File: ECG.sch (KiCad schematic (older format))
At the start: 14 parts, among them P1 MountingHole_Pad, P2 MountingHole_Pad, P3 MountingHole_Pad, U1 ADR4525, U2 L7805

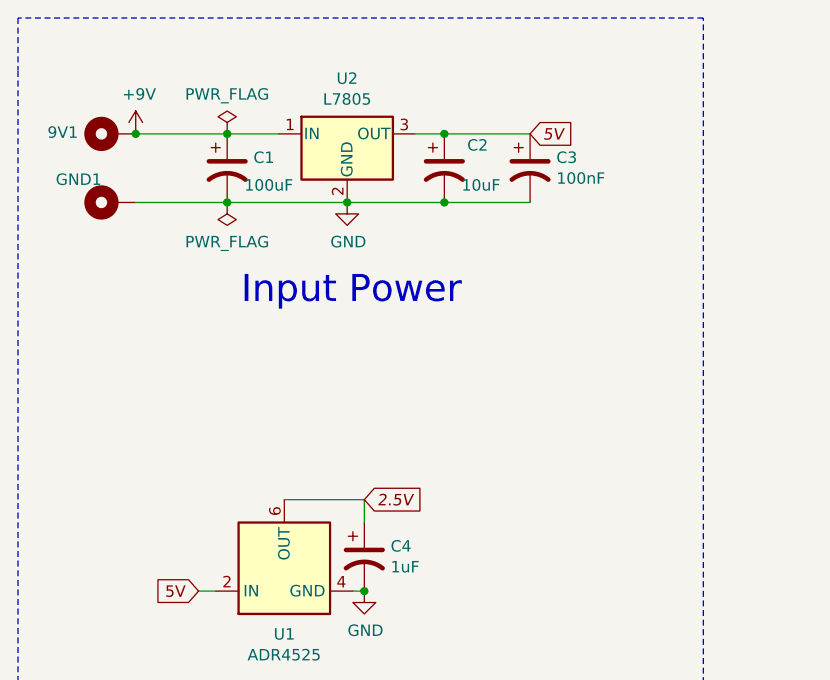
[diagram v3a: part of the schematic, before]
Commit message: Added battery circuit
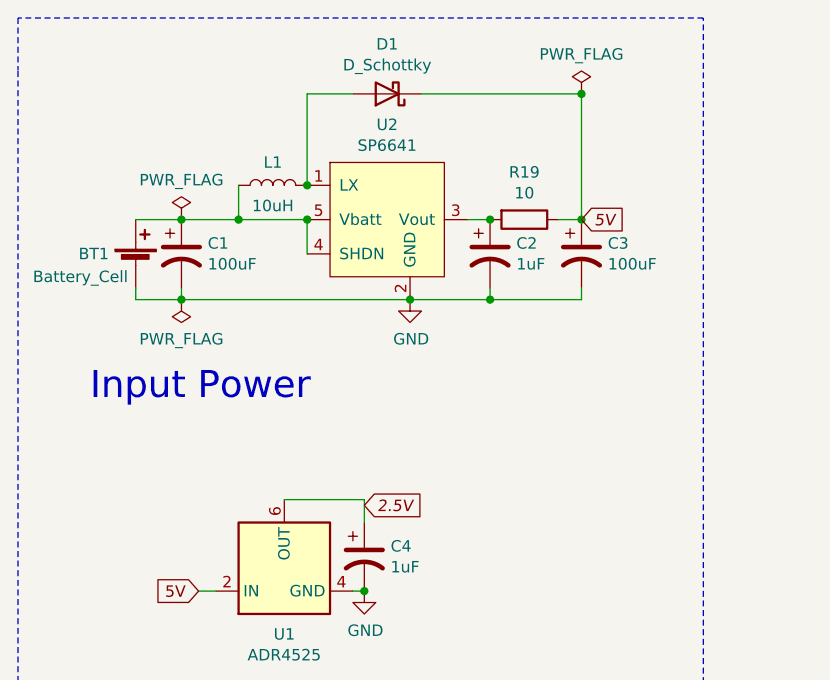
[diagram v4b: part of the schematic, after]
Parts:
- removed 9V1: MountingHole_Pad, MountingHole:MountingHole_6.5mm_Pad_Via, symbol Mechanical:MountingHole_Pad
- removed GND1: MountingHole_Pad, MountingHole:MountingHole_6mm_Pad_Via, symbol Mechanical:MountingHole_Pad
- removed U2: L7805, Package_TO_SOT_THT:TO-220-3_Horizontal_TabDown, symbol Regulator_Linear:L7805
- added BT1: Battery_Cell, symbol Device:Battery_Cell
- added D1: D_Schottky, Diode_SMD:D_SOD-323_HandSoldering, symbol Device:D_Schottky
- added L1: 10uH, symbol Device:L
- added R19: 10, Resistor_SMD:R_0805_2012Metric_Pad1.15x1.40mm_HandSolder, symbol Device:R
- added U2: SP6641, symbol Regulators:SP6641
- C1: footprint Capacitor_SMD:CP_Elec_6.3x3 -> Capacitor_SMD:C_0805_2012Metric_Pad1.15x1.40mm_HandSolder
- C2: value 10uF -> 1uF; footprint Capacitor_SMD:CP_Elec_5x5.3 -> Capacitor_SMD:C_0805_2012Metric_Pad1.15x1.40mm_HandSolder
- C3: value 100nF -> 100uF
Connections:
- net 5V: now also D1.1 (K), R19.1; no longer C2.1
- net GND: now also BT1.2 (-), U2.2 (GND)
- net +9V: no longer names the net of C1.1
- net +9V: now also BT1.1 (+), L1.1, U2.4 (SHDN), U2.5 (Vbatt)
- new net: D1.2 (A), L1.2, U2.1 (LX)
- new net: C2.1, R19.2, U2.3 (Vout)
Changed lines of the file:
@@
 Comment4 ""
 $EndDescr
-$Comp
-L Device:CP1 C2
-U 1 1 5F980DB6
-P 2750 2425
-F 0 "C2" H 2850 2525 50  0000 L CNN
-F 1 "10uF" H 2825 2350 50  0000 L CNN
-F 2 "Capacitor_SMD:CP_Elec_5x5.3" H 2750 2425 50  0001 C CNN
-F 3 "https://www.illinoiscapacitor.com/pdf/seriesDocuments/AXZ%20series.pdf" H 2750 2425 50  0001 C CNN
-	1    2750 2425
-	1    0    0    -1
-$EndComp
-$Comp
-L Device:CP1 C3
-U 1 1 5F9833A5
-P 3125 2425
-F 0 "C3" H 3240 2471 50  0000 L CNN
-F 1 "100nF" H 3240 2380 50  0000 L CNN
-F 2 "Capacitor_SMD:C_0805_2012Metric_Pad1.15x1.40mm_HandSolder" H 3125 2425 50  0001 C CNN
-F 3 "~" H 3125 2425 50  0001 C CNN
-	1    3125 2425
-	1    0    0    -1
-$EndComp
-$Comp
-L Mechanical:MountingHole_Pad 9V1
-U 1 1 5F985E28
-P 1300 2275
-F 0 "9V1" V 1306 2427 50  0000 L CNN
-F 1 "MountingHole_Pad" V 1400 2233 50  0001 L CNN
-F 2 "MountingHole:MountingHole_6.5mm_Pad_Via" H 1300 2275 50  0001 C CNN
-F 3 "~" H 1300 2275 50  0001 C CNN
-	1    1300 2275
-	0    -1   -1   0
-$EndComp
-$Comp
-L Mechanical:MountingHole_Pad GND1
-U 1 1 5F98A564
-P 1300 2575
-F 0 "GND1" V 1400 2624 50  0000 L CNN
-F 1 "MountingHole_Pad" V 1400 2533 50  0001 L CNN
-F 2 "MountingHole:MountingHole_6mm_Pad_Via" H 1300 2575 50  0001 C CNN
-F 3 "~" H 1300 2575 50  0001 C CNN
-	1    1300 2575
-	0    -1   -1   0
-$EndComp
-Text Notes 1861 3030 0    118  ~ 0
+Text Notes 1200 3450 0    118  ~ 0
 Input Power
 Text Notes 1733 4734 0    50   ~ 0
@@
 Wire Notes Line
 	885  1768 885  1998
-$Comp
-L power:GND #PWR0102
-U 1 1 5F9A88EF
-P 2325 2575
-F 0 "#PWR0102" H 2325 2325 50  0001 C CNN
-F 1 "GND" H 2330 2402 50  0000 C CNN
-F 2 "" H 2325 2575 50  0001 C CNN
-F 3 "" H 2325 2575 50  0001 C CNN
-	1    2325 2575
-	1    0    0    -1
-$EndComp
-$Comp
-L power:+9V #PWR0101
-U 1 1 5F9AB243
-P 1400 2275
-F 0 "#PWR0101" H 1400 2125 50  0001 C CNN
-F 1 "+9V" H 1415 2448 50  0000 C CNN
-F 2 "" H 1400 2275 50  0001 C CNN
-F 3 "" H 1400 2275 50  0001 C CNN
-	1    1400 2275
-	1    0    0    -1
-$EndComp
-$Comp
-L power:PWR_FLAG #FLG01
-U 1 1 5F9B3B5D
-P 1800 2275
-F 0 "#FLG01" H 1800 2350 50  0001 C CNN
-F 1 "PWR_FLAG" H 1800 2448 50  0000 C CNN
-F 2 "" H 1800 2275 50  0001 C CNN
-F 3 "~" H 1800 2275 50  0001 C CNN
-	1    1800 2275
-	1    0    0    -1
-$EndComp
 $Comp
 L Device:CP1 C4
@@
 	1    0    0    -1
 $EndComp
-$Comp
-L Regulator_Linear:L7805 U2
-U 1 1 5F977B65
-P 2325 2275
-F 0 "U2" H 2325 2517 50  0000 C CNN
-F 1 "L7805" H 2325 2426 50  0000 C CNN
-F 2 "Package_TO_SOT_THT:TO-220-3_Horizontal_TabDown" H 2350 2125 50  0001 L CIN
-F 3 "http://www.st.com/content/ccc/resource/technical/document/datasheet/41/4f/b3/b0/12/d4/47/88/CD00000444.pdf/files/CD00000444.pdf/jcr:content/translations/en.CD00000444.pdf" H 2325 2225 50  0001 C CNN
-	1    2325 2275
-	1    0    0    -1
-$EndComp
-$Comp
-L Device:CP1 C1
-U 1 1 5F97B8CA
-P 1800 2425
-F 0 "C1" H 1915 2471 50  0000 L CNN
-F 1 "100uF" H 1875 2350 50  0000 L CNN
-F 2 "Capacitor_SMD:CP_Elec_6.3x3" H 1800 2425 50  0001 C CNN
-F 3 "https://www.we-online.de/katalog/datasheet/860240575006.pdf" H 1800 2425 50  0001 C CNN
-	1    1800 2425
-	1    0    0    -1
-$EndComp
-Wire Wire Line
-	1400 2575 1800 2575
-Connection ~ 1800 2575
-Wire Wire Line
-	2325 2575 1800 2575
-Connection ~ 2325 2575
-Wire Wire Line
-	1800 2275 1400 2275
-Connection ~ 1800 2275
-Connection ~ 1400 2275
-Wire Wire Line
-	1800 2275 2025 2275
-Wire Wire Line
-	2625 2275 2750 2275
-Wire Wire Line
-	2325 2575 2750 2575
-Wire Wire Line
-	3125 2575 2750 2575
-Connection ~ 2750 2575
-Wire Wire Line
-	3125 2275 2750 2275
-Connection ~ 2750 2275
-Text GLabel 3125 2275 2    50   Input Italic 0
+Text GLabel 3350 2650 2    50   Input Italic 0
 5V
 Wire Wire Line
 	2350 4275 2400 4275
 Connection ~ 2400 4275
-$Comp
-L power:PWR_FLAG #FLG0101
-U 1 1 5F9F7887
-P 1800 2575
-F 0 "#FLG0101" H 1800 2650 50  0001 C CNN
-F 1 "PWR_FLAG" H 1800 2748 50  0000 C CNN
-F 2 "" H 1800 2575 50  0001 C CNN
-F 3 "~" H 1800 2575 50  0001 C CNN
-	1    1800 2575
-	-1   0    0    1
-$EndComp
 $Sheet
 S 6425 2800 950  1425
@@
 F3 "Vin" I L 8375 3500 50
 $EndSheet
-Text GLabel 2400 3875 2    50   Input Italic 0
+Text GLabel 2400 3900 2    50   Input Italic 0
 2.5V
 Wire Wire Line
@@
 	0    1    1    0
 $EndComp
+$Comp
+L Regulators:SP6641 U2
+U 1 1 5FB1FB38
+P 2500 2350
+F 0 "U2" H 2500 2465 50  0000 C CNN
+F 1 "SP6641" H 2500 2374 50  0000 C CNN
+F 2 "" H 2500 2350 50  0001 C CNN
+F 3 "https://www.maxlinear.com/ds/sp6641_100_052605.pdf" H 2500 2350 50  0001 C CNN
+	1    2500 2350
+	1    0    0    -1
+$EndComp
+$Comp
+L Device:L L1
+U 1 1 5FB201C3
+P 2000 2500
+F 0 "L1" V 2100 2500 50  0000 C CNN
+F 1 "10uH" V 1910 2500 50  0000 C CNN
+F 2 "" H 2000 2500 50  0001 C CNN
+F 3 "products.sumida.com/products/pdf/CDRH5D28.pdf" H 2000 2500 50  0001 C CNN
+	1    2000 2500
+	0    -1   -1   0
+$EndComp
+$Comp
+L Device:D_Schottky D1
+U 1 1 5FB221FB
+P 2500 2100
+F 0 "D1" H 2500 1883 50  0000 C CNN
+F 1 "D_Schottky" H 2500 1974 50  0000 C CNN
+F 2 "Diode_SMD:D_SOD-323_HandSoldering" H 2500 2100 50  0001 C CNN
+F 3 "https://toshiba.semicon-storage.com/info/docget.jsp?did=14564&prodName=CUS10S40" H 2500 2100 50  0001 C CNN
+	1    2500 2100
+	-1   0    0    1
+$EndComp
+$Comp
+L Device:CP1 C1
+U 1 1 5FB22A08
+P 1600 2800
+F 0 "C1" H 1715 2846 50  0000 L CNN
+F 1 "100uF" H 1715 2755 50  0000 L CNN
+F 2 "Capacitor_SMD:C_0805_2012Metric_Pad1.15x1.40mm_HandSolder" H 1600 2800 50  0001 C CNN
+F 3 "~" H 1600 2800 50  0001 C CNN
+	1    1600 2800
+	1    0    0    -1
+$EndComp
+$Comp
+L Device:CP1 C3
+U 1 1 5FB22EA7
+P 3350 2800
+F 0 "C3" H 3465 2846 50  0000 L CNN
+F 1 "100uF" H 3465 2755 50  0000 L CNN
+F 2 "Capacitor_SMD:C_0805_2012Metric_Pad1.15x1.40mm_HandSolder" H 3350 2800 50  0001 C CNN
+F 3 "~" H 3350 2800 50  0001 C CNN
+	1    3350 2800
+	1    0    0    -1
+$EndComp
+$Comp
+L Device:CP1 C2
+U 1 1 5FB23B17
+P 2950 2800
+F 0 "C2" H 3065 2846 50  0000 L CNN
+F 1 "1uF" H 3065 2755 50  0000 L CNN
+F 2 "Capacitor_SMD:C_0805_2012Metric_Pad1.15x1.40mm_HandSolder" H 2950 2800 50  0001 C CNN
+F 3 "~" H 2950 2800 50  0001 C CNN
+	1    2950 2800
+	1    0    0    -1
+$EndComp
+$Comp
+L Device:R R19
+U 1 1 5FB24D04
+P 3100 2650
+F 0 "R19" V 2893 2650 50  0000 C CNN
+F 1 "10" V 2984 2650 50  0000 C CNN
+F 2 "Resistor_SMD:R_0805_2012Metric_Pad1.15x1.40mm_HandSolder" V 3030 2650 50  0001 C CNN
+F 3 "~" H 3100 2650 50  0001 C CNN
+	1    3100 2650
+	0    1    1    0
+$EndComp
+$Comp
+L Device:Battery_Cell BT1
+U 1 1 5FB28E21
+P 1400 2850
+F 0 "BT1" H 1150 2900 50  0000 L CNN
+F 1 "Battery_Cell" H 950 2800 50  0000 L CNN
+F 2 "" V 1400 2910 50  0001 C CNN
+F 3 "~" V 1400 2910 50  0001 C CNN
+	1    1400 2850
+	1    0    0    -1
+$EndComp
+Wire Wire Line
+	2150 2650 2150 2800
+Connection ~ 2150 2650
+Wire Wire Line
+	1400 2650 1600 2650
+$Comp
+L power:GND #PWR010
+U 1 1 5FB392BD
+P 2600 3000
+F 0 "#PWR010" H 2600 2750 50  0001 C CNN
+F 1 "GND" H 2605 2827 50  0000 C CNN
+F 2 "" H 2600 3000 50  0001 C CNN
+F 3 "" H 2600 3000 50  0001 C CNN
+	1    2600 3000
+	1    0    0    -1
+$EndComp
+Connection ~ 2600 3000
+Wire Wire Line
+	1400 2950 1400 3000
+Connection ~ 1600 2650
+Wire Wire Line
+	1400 3000 1600 3000
+Wire Wire Line
+	1600 2650 1850 2650
+Wire Wire Line
+	1600 2950 1600 3000
+Connection ~ 1600 3000
+Wire Wire Line
+	1600 3000 2600 3000
+Wire Wire Line
+	1850 2500 1850 2650
+Connection ~ 1850 2650
+Wire Wire Line
+	1850 2650 2150 2650
+Wire Wire Line
+	2150 2500 2150 2100
+Wire Wire Line
+	2150 2100 2350 2100
+Connection ~ 2150 2500
+Wire Wire Line
+	2650 2100 3350 2100
+Wire Wire Line
+	3350 2100 3350 2650
+Wire Wire Line
+	3350 2650 3250 2650
+Wire Wire Line
+	2950 2650 2850 2650
+Connection ~ 2950 2650
+Wire Wire Line
+	2600 3000 2950 3000
+Wire Wire Line
+	2950 3000 2950 2950
+Connection ~ 3350 2650
+Wire Wire Line
+	3350 2950 3350 3000
+Wire Wire Line
+	3350 3000 2950 3000
+Connection ~ 2950 3000
+$Comp
+L power:PWR_FLAG #FLG0101
+U 1 1 5FB7CDDB
+P 1600 2650
+F 0 "#FLG0101" H 1600 2725 50  0001 C CNN
+F 1 "PWR_FLAG" H 1600 2823 50  0000 C CNN
+F 2 "" H 1600 2650 50  0001 C CNN
+F 3 "~" H 1600 2650 50  0001 C CNN
+	1    1600 2650
+	1    0    0    -1
+$EndComp
+$Comp
+L power:PWR_FLAG #FLG0102
+U 1 1 5FB7CFF8
+P 1600 3000
+F 0 "#FLG0102" H 1600 3075 50  0001 C CNN
+F 1 "PWR_FLAG" H 1600 3173 50  0000 C CNN
+F 2 "" H 1600 3000 50  0001 C CNN
+F 3 "~" H 1600 3000 50  0001 C CNN
+	1    1600 3000
+	-1   0    0    1
+$EndComp
+$Comp
+L power:PWR_FLAG #FLG0103
+U 1 1 5FB7FFA0
+P 3350 2100
+F 0 "#FLG0103" H 3350 2175 50  0001 C CNN
+F 1 "PWR_FLAG" H 3350 2273 50  0000 C CNN
+F 2 "" H 3350 2100 50  0001 C CNN
+F 3 "~" H 3350 2100 50  0001 C CNN
+	1    3350 2100
+	1    0    0    -1
+$EndComp
+Connection ~ 3350 2100
 $EndSCHEMATC

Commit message: #1 - Create PCB footprints
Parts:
- BT1: footprint (none) -> Battery:BatteryHolder_Keystone_3008_1x2450
- C1, C3: footprint Capacitor_SMD:C_0805_2012Metric_Pad1.15x1.40mm_HandSolder -> Capacitor_SMD:CP_Elec_6.3x5.3
- L1: footprint (none) -> Inductors:L_Sumida_CDRH5D28
- U2: footprint (none) -> Package_TO_SOT_SMD:SOT-23-5
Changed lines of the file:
@@
 F 0 "U2" H 2500 2465 50  0000 C CNN
 F 1 "SP6641" H 2500 2374 50  0000 C CNN
-F 2 "" H 2500 2350 50  0001 C CNN
+F 2 "Package_TO_SOT_SMD:SOT-23-5" H 2500 2350 50  0001 C CNN
 F 3 "https://www.maxlinear.com/ds/sp6641_100_052605.pdf" H 2500 2350 50  0001 C CNN
 	1    2500 2350
@@
 F 0 "L1" V 2100 2500 50  0000 C CNN
 F 1 "10uH" V 1910 2500 50  0000 C CNN
-F 2 "" H 2000 2500 50  0001 C CNN
+F 2 "Inductors:L_Sumida_CDRH5D28" H 2000 2500 50  0001 C CNN
 F 3 "products.sumida.com/products/pdf/CDRH5D28.pdf" H 2000 2500 50  0001 C CNN
 	1    2000 2500
@@
 F 0 "C1" H 1715 2846 50  0000 L CNN
 F 1 "100uF" H 1715 2755 50  0000 L CNN
-F 2 "Capacitor_SMD:C_0805_2012Metric_Pad1.15x1.40mm_HandSolder" H 1600 2800 50  0001 C CNN
+F 2 "Capacitor_SMD:CP_Elec_6.3x5.3" H 1600 2800 50  0001 C CNN
 F 3 "~" H 1600 2800 50  0001 C CNN
 	1    1600 2800
@@
 F 0 "C3" H 3465 2846 50  0000 L CNN
 F 1 "100uF" H 3465 2755 50  0000 L CNN
-F 2 "Capacitor_SMD:C_0805_2012Metric_Pad1.15x1.40mm_HandSolder" H 3350 2800 50  0001 C CNN
+F 2 "Capacitor_SMD:CP_Elec_6.3x5.3" H 3350 2800 50  0001 C CNN
 F 3 "~" H 3350 2800 50  0001 C CNN
 	1    3350 2800
@@
 F 0 "BT1" H 1150 2900 50  0000 L CNN
 F 1 "Battery_Cell" H 950 2800 50  0000 L CNN
-F 2 "" V 1400 2910 50  0001 C CNN
+F 2 "Battery:BatteryHolder_Keystone_3008_1x2450" V 1400 2910 50  0001 C CNN
 F 3 "~" V 1400 2910 50  0001 C CNN
 	1    1400 2850
